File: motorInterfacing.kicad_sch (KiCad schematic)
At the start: 6 parts, among them J1 Conn_01x02, J2 Conn_01x02, J3 Conn_01x01, J4 Conn_01x01

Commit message: created PCB and layout
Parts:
- removed C21: 330u, Capacitor_SMD:C_0603_1608Metric, symbol Device:C_Polarized_Small
- removed J2: Conn_01x02, symbol Connector_Generic:Conn_01x02
- removed J4: Conn_01x01, symbol Connector_Generic:Conn_01x01
- added C26: 1uF, Capacitor_SMD:C_0603_1608Metric, symbol Device:C_Small
- J1: footprint (none) -> Connector_AMASS:AMASS_XT30U-F_1x02_P5.0mm_Vertical
- J3: footprint (none) -> Connector_Wire:SolderWire-0.5sqmm_1x01_D0.9mm_OD2.1mm
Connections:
- net +BATT: now also C26.1
- net GND: now also C26.2
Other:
- note added: "DS51150 — Fullscale Motor and REEFS119 - Subscale Motor (Same interface, will switch the motors after subscale is odne)"
- note removed: "DS51150 — Fullscale Motor"
- note removed: "Make sure capacitors are rated"
- note removed: "REEFS119 — Subscale Motor"

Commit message: Fixed capacitor placement
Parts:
- C25: footprint Capacitor_SMD:C_0603_1608Metric -> Capacitor_SMD:CP_Elec_6.3x9.9
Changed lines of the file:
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@@
 			)
 		)
-		(property "Footprint" "Capacitor_SMD:C_0603_1608Metric"
+		(property "Footprint" "Capacitor_SMD:CP_Elec_6.3x9.9"
 			(at 92.075 76.835 0)
 			(hide yes)

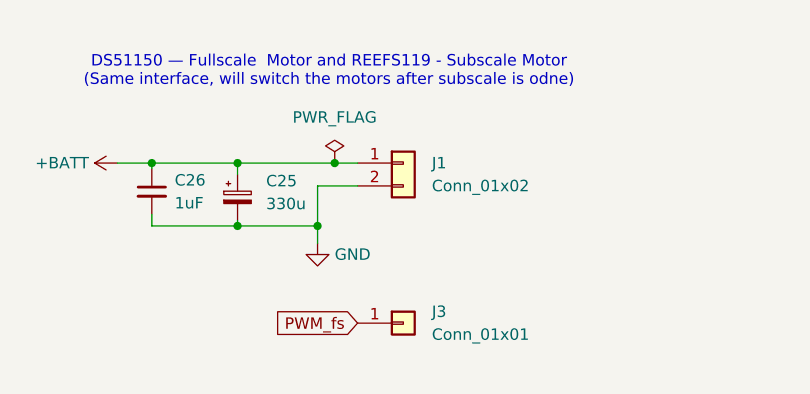
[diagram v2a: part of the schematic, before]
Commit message: Redid Footprints/Picked components
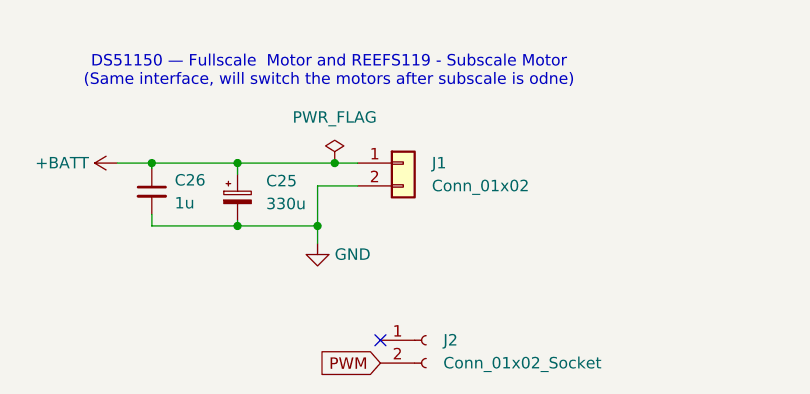
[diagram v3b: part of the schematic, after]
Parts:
- removed J3: Conn_01x01, Connector_Wire:SolderWire-0.5sqmm_1x01_D0.9mm_OD2.1mm, symbol Connector_Generic:Conn_01x01
- added J2: Conn_01x02_Socket, Connector_JST:JST_VH_B2P-VH-B_1x02_P3.96mm_Vertical, symbol Connector:Conn_01x02_Socket
- C26: value 1uF -> 1u; footprint Capacitor_SMD:C_0603_1608Metric -> Capacitor_SMD:C_0805_2012Metric
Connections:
- new net PWM: J2.2 (Pin_2)
- no-connect marks 0 -> 1
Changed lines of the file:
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@@
 		(color 0 0 0 0)
 	)
+	(no_connect
+		(at 107.95 92.71)
+	)
 	(wire
 		(pts
@@
 		)
 	)
-	(global_label "PWM_fs"
+	(global_label "PWM"
 		(shape input)
-		(at 105.41 90.805 180)
+		(at 107.95 95.25 180)
 		(fields_autoplaced yes)
 		(effects
@@
 		)
 		(property "Intersheetrefs" "${INTERSHEET_REFS}"
-			(at 95.5306 90.805 0)
+			(at 100.792 95.25 0)
 			(hide yes)
 			(show_name no)
@@
 	)
 	(symbol
+		(lib_id "Connector:Conn_01x02_Socket")
+		(at 113.03 92.71 0)
+		(unit 1)
+		(body_style 1)
+		(exclude_from_sim no)
+		(in_bom yes)
+		(on_board yes)
+		(in_pos_files yes)
+		(dnp no)
+		(fields_autoplaced yes)
+		(property "Reference" "J2"
+			(at 114.935 92.7099 0)
+			(show_name no)
+			(do_not_autoplace no)
+			(effects
+				(font
+					(size 1.27 1.27)
+				)
+				(justify left)
+			)
+		)
+		(property "Value" "Conn_01x02_Socket"
+			(at 114.935 95.2499 0)
+			(show_name no)
+			(do_not_autoplace no)
+			(effects
+				(font
+					(size 1.27 1.27)
+				)
+				(justify left)
+			)
+		)
+		(property "Footprint" "Connector_JST:JST_VH_B2P-VH-B_1x02_P3.96mm_Vertical"
+			(at 113.03 92.71 0)
+			(hide yes)
+			(show_name no)
+			(do_not_autoplace no)
+			(effects
+				(font
+					(size 1.27 1.27)
+				)
+			)
+		)
+		(property "Datasheet" ""
+			(at 113.03 92.71 0)
+			(hide yes)
+			(show_name no)
+			(do_not_autoplace no)
+			(effects
+				(font
+					(size 1.27 1.27)
+				)
+			)
+		)
+		(property "Description" "Generic connector, single row, 01x02, script generated"
+			(at 113.03 92.71 0)
+			(hide yes)
+			(show_name no)
+			(do_not_autoplace no)
+			(effects
+				(font
+					(size 1.27 1.27)
+				)
+			)
+		)
+		(pin "2"
+		)
+		(pin "1"
+		)
+		(instances
+			(project "ACS PCB"
+				(path "/67a598cb-afc0-4277-b58a-8f35d31efc48/40a97d9b-8926-4155-910d-2a9118abe21d"
+					(reference "J2")
+					(unit 1)
+				)
+			)
+		)
+	)
+	(symbol
 		(lib_id "power:+BATT")
 		(at 78.74 73.025 90)
@@
 			)
 		)
-		(property "Value" "1uF"
+		(property "Value" "1u"
 			(at 85.09 77.4762 0)
 			(show_name no)
@@
 			)
 		)
-		(property "Footprint" "Capacitor_SMD:C_0603_1608Metric"
+		(property "Footprint" "Capacitor_SMD:C_0805_2012Metric"
 			(at 82.55 76.2 0)
 			(hide yes)
@@
 					(unit 1)
 				)
-			)
-		)
-	)
-	(symbol
-		(lib_id "Connector_Generic:Conn_01x01")
-		(at 110.49 90.805 0)
-		(unit 1)
-		(body_style 1)
-		(exclude_from_sim no)
-		(in_bom yes)
-		(on_board yes)
-		(in_pos_files yes)
-		(dnp no)
-		(fields_autoplaced yes)
-		(property "Reference" "J3"
-			(at 113.665 89.5349 0)
-			(show_name no)
-			(do_not_autoplace no)
-			(effects
-				(font
-					(size 1.27 1.27)
-				)
-				(justify left)
-			)
-		)
-		(property "Value" "Conn_01x01"
-			(at 113.665 92.0749 0)
-			(show_name no)
-			(do_not_autoplace no)
-			(effects
-				(font
-					(size 1.27 1.27)
-				)
-				(justify left)
-			)
-		)
-		(property "Footprint" "Connector_Wire:SolderWire-0.5sqmm_1x01_D0.9mm_OD2.1mm"
-			(at 110.49 90.805 0)
-			(hide yes)
-			(show_name no)
-			(do_not_autoplace no)
-			(effects
-				(font
-					(size 1.27 1.27)
-				)
-			)
-		)
-		(property "Datasheet" ""
-			(at 110.49 90.805 0)
-			(hide yes)
-			(show_name no)
-			(do_not_autoplace no)
-			(effects
-				(font
-					(size 1.27 1.27)
-				)
-			)
-		)
-		(property "Description" "Generic connector, single row, 01x01, script generated (kicad-library-utils/schlib/autogen/connector/)"
-			(at 110.49 90.805 0)
-			(hide yes)
-			(show_name no)
-			(do_not_autoplace no)
-			(effects
-				(font
-					(size 1.27 1.27)
-				)
-			)
-		)
-		(pin "1"
-		)
-		(instances
-			(project "ACS PCB"
-				(path "/67a598cb-afc0-4277-b58a-8f35d31efc48/40a97d9b-8926-4155-910d-2a9118abe21d"
-					(reference "J3")
-					(unit 1)
-				)
